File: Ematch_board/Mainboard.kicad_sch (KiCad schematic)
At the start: 69 parts, among them J10 Conn_01x02_Male, J11 Conn_Coaxial, J7 RBUS, J8 USB_C_Receptacle_USB2.0, J9 Conn_01x02_Male, Q1 MMDT2222A, U2 LTC4411, U3 SC4216H, U4 LTC4411, U5 SN65HVD230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

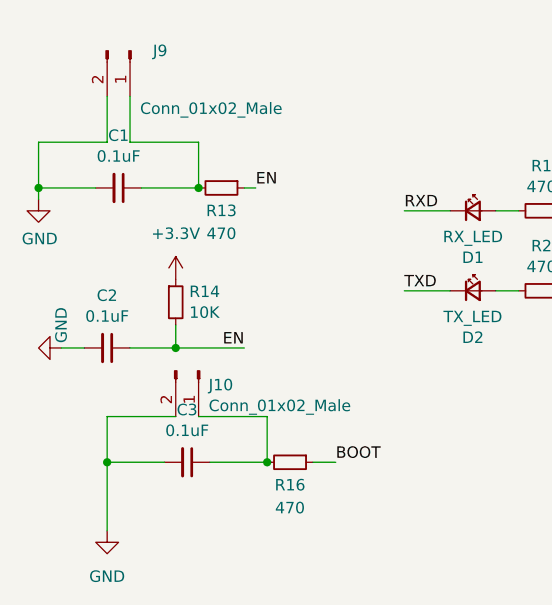
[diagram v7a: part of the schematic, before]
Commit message: Changed autoprogrammer caps to 1uF
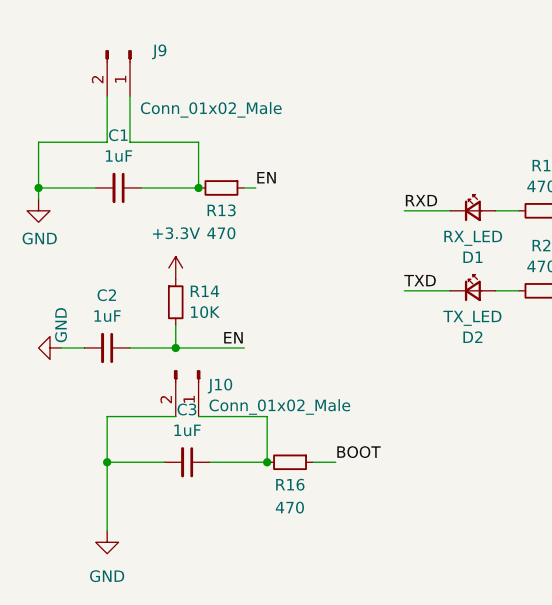
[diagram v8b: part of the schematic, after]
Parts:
- C1, C2, C3: value 0.1uF -> 1uF
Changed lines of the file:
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@@
     (in_bom yes) (on_board yes)
     (property "Reference" "C3" (id 0) (at -6.35 39.9034 90))
-    (property "Value" "0.1uF" (id 1) (at -6.35 42.2148 90))
+    (property "Value" "1uF" (id 1) (at -6.35 42.2148 90))
     (property "Footprint" "Capacitor_SMD:C_0603_1608Metric" (id 2) (at -6.35 45.72 0)
       (effects (font (size 1.27 1.27)) hide)
@@
     (in_bom yes) (on_board yes)
     (property "Reference" "C1" (id 0) (at -13.97 9.4234 90))
-    (property "Value" "0.1uF" (id 1) (at -13.97 11.7348 90))
+    (property "Value" "1uF" (id 1) (at -13.97 11.7348 90))
     (property "Footprint" "Capacitor_SMD:C_0603_1608Metric" (id 2) (at -13.97 15.24 0)
       (effects (font (size 1.27 1.27)) hide)
@@
     (in_bom yes) (on_board yes)
     (property "Reference" "C2" (id 0) (at -15.24 27.2034 90))
-    (property "Value" "0.1uF" (id 1) (at -15.24 29.5148 90))
+    (property "Value" "1uF" (id 1) (at -15.24 29.5148 90))
     (property "Footprint" "Capacitor_SMD:C_0603_1608Metric" (id 2) (at -15.24 33.02 0)
       (effects (font (size 1.27 1.27)) hide)
@@
     )
     (path "/00000000-0000-0000-0000-00005dabbfe7"
-      (reference "C1") (unit 1) (value "0.1uF") (footprint "Capacitor_SMD:C_0603_1608Metric")
+      (reference "C1") (unit 1) (value "1uF") (footprint "Capacitor_SMD:C_0603_1608Metric")
     )
     (path "/7468b08c-11d4-40e8-94cc-5b8536475a97"
-      (reference "C2") (unit 1) (value "0.1uF") (footprint "Capacitor_SMD:C_0603_1608Metric")
+      (reference "C2") (unit 1) (value "1uF") (footprint "Capacitor_SMD:C_0603_1608Metric")
     )
     (path "/00000000-0000-0000-0000-00005dab5946"
-      (reference "C3") (unit 1) (value "0.1uF") (footprint "Capacitor_SMD:C_0603_1608Metric")
+      (reference "C3") (unit 1) (value "1uF") (footprint "Capacitor_SMD:C_0603_1608Metric")
     )
     (path "/3d0c5cc1-3a97-4ec3-9ebe-7262bf5dcc3c"
